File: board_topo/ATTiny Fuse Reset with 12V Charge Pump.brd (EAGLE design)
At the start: 68.6 x 53.3 mm, 59 parts, among them IC1 74HC04D, Q1 BSS138, Q2 PMV65XP, Q3 BSS138, Q4 BSS138, Q5 BSS138, Q6 BSS138, Q7 BSS138, Q8 BSS130, SW3 SWITCH_SPDT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

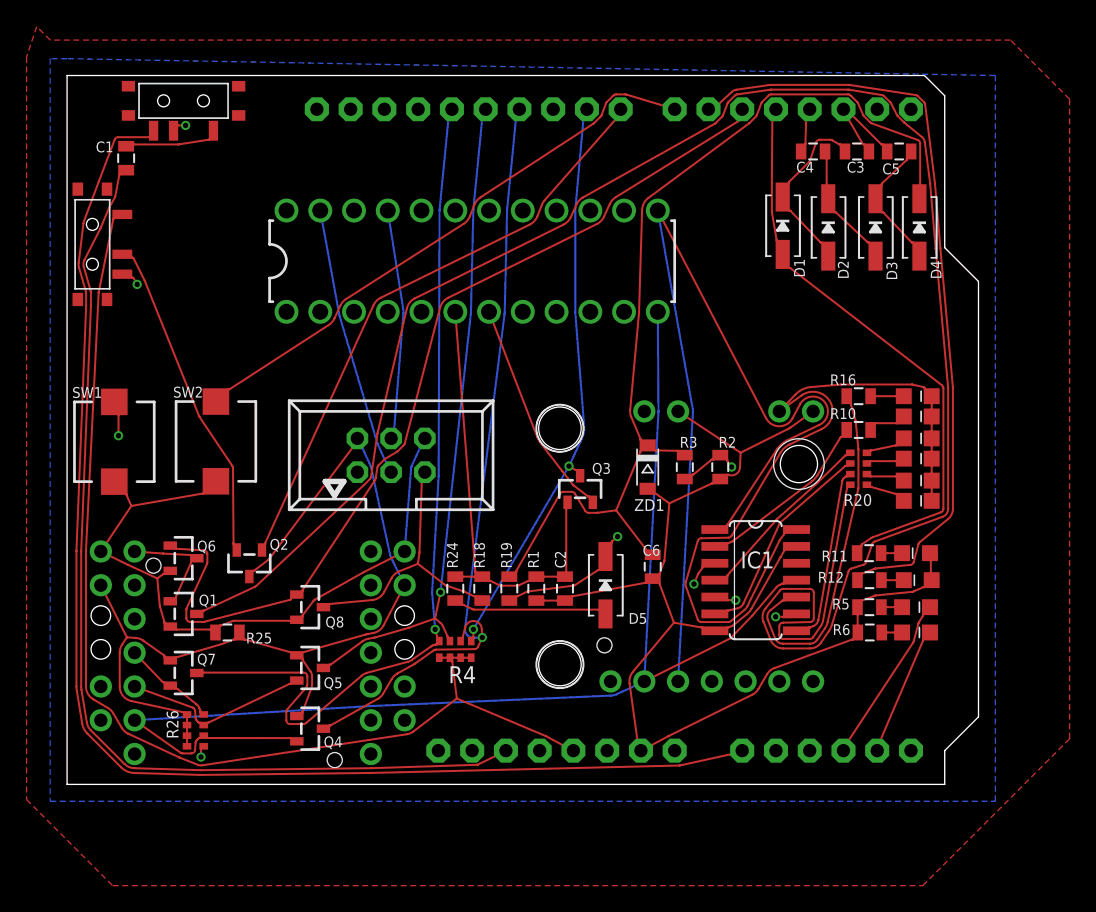
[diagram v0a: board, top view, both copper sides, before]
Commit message: new brd with 4layer, tnames fix
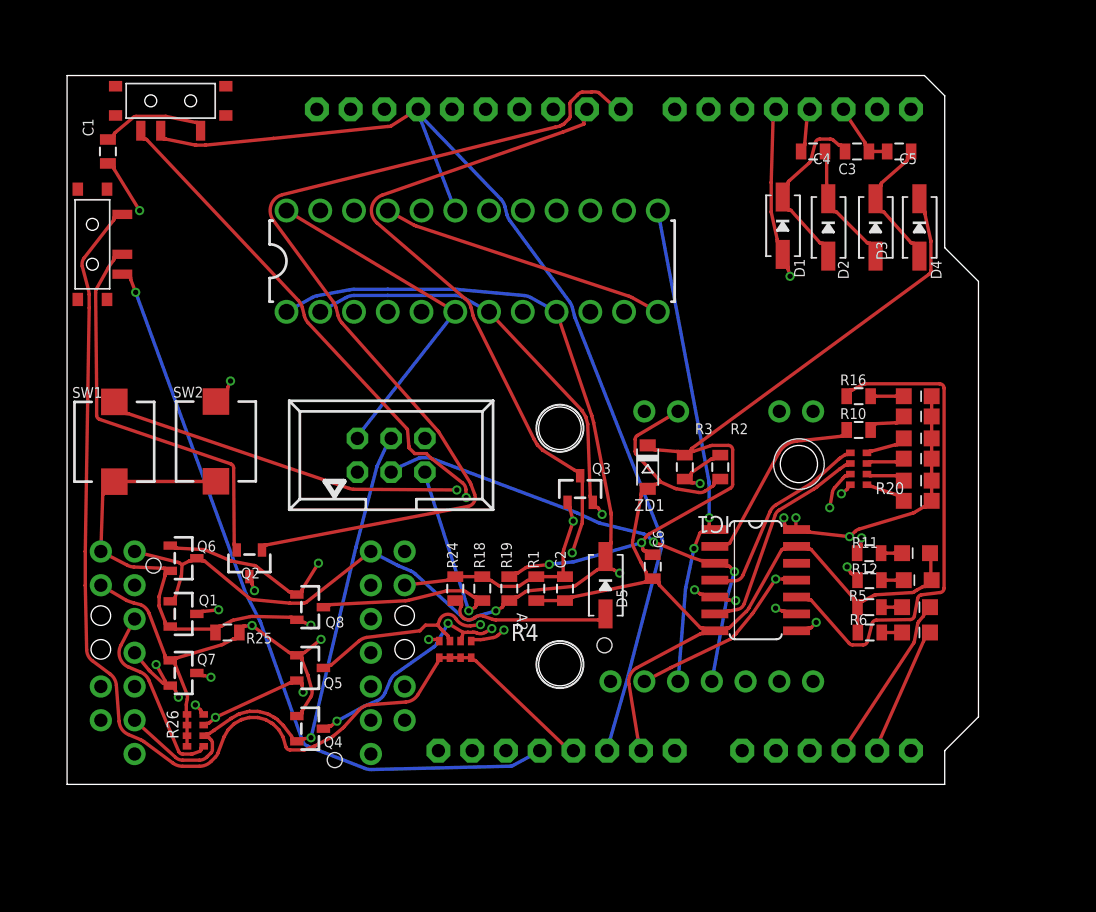
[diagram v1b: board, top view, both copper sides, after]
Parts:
- HV_ON: value HV -> HV on
- ISP: value pmd -> pmode
- PB5: value PB5 -> PB5 rst
- moved C1 1.46 mm to (3.07, 47.6)
- moved SW3 0.97 mm to (7.80, 51.4)
- renumbered HVON to HV_ON
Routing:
- net N$32: track 149.9 -> 51.2 mm, vias 0 -> 2
- net ATTINY_VCC: track 247.7 -> 161.8 mm, vias 0 -> 7
- net SII-MISO: track 150.1 -> 109.0 mm, vias 0 -> 4
- net SCI: track 127.8 -> 91.0 mm, vias 2 -> 3
- net N$3: track 99.2 -> 65.5 mm, vias 0 -> 1
- net VCC_OFF: track 44.6 -> 72.2 mm
- net GND: track 237.6 -> 264.7 mm
- net N$19: track 57.6 -> 36.6 mm, vias 0 -> 1
- net N$33: track 75.8 -> 56.2 mm, vias 0 -> 1
- net SDI_MOSI: track 133.5 -> 115.7 mm, vias 0 -> 2
- net N$2: track 43.5 -> 60.0 mm
- net 11.5V: track 73.7 -> 58.2 mm, vias 0 -> 2
- net HV/RESET: track 117.3 -> 103.1 mm, vias 1 -> 2
- net N$13: track 26.8 -> 38.2 mm
- net PUMP_VCC: track 43.6 -> 33.6 mm, vias 0 -> 2
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- removed copper zone on layer 1, net GND
- removed copper zone on layer 16, net GND
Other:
- board text removed: "ATTiny Fuse Reset with 12V Charge Pump Programmer"
- board text removed: "TAMI.org.il"
- board text removed: "V001 05/08/2015 TAMI.org.il"

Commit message: fixied traces in 4layer board, version in board-topor go to fab
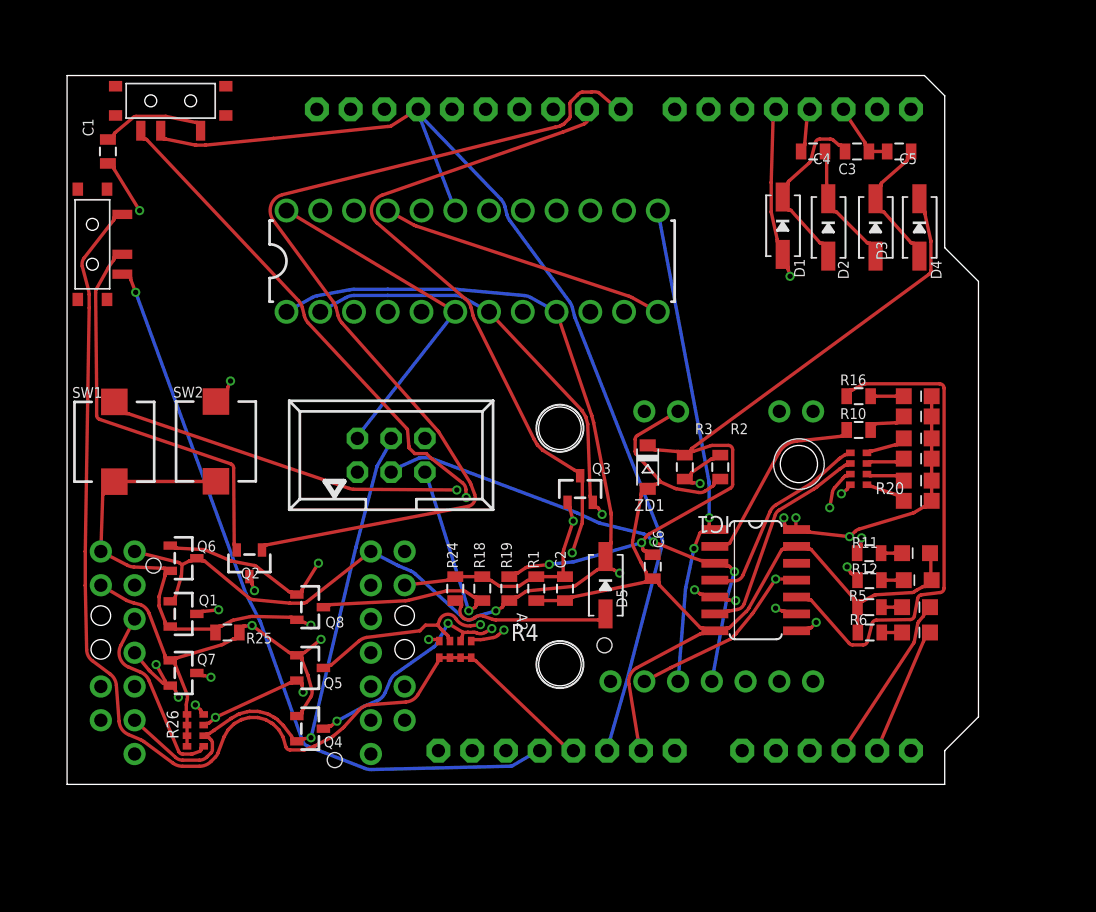
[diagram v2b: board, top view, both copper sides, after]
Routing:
- net GND: track 264.7 -> 271.8 mm
- net ATTINY_VCC: track 161.8 -> 164.2 mm
- net SDO-SCK: track 110.2 -> 112.4 mm
- net SDI_MOSI: track 115.7 -> 117.2 mm
- net N$2: track 60.0 -> 61.0 mm
- net HV_OFF(RESET): track 59.8 -> 60.8 mm
- net P2: track 2.42 -> 3.34 mm
- net N$8: track 56.4 -> 57.3 mm
- net N$37: track 53.3 -> 54.3 mm
- net N$33: track 56.2 -> 57.1 mm
- net N$16: track 55.7 -> 56.6 mm
- net N$19: track 36.6 -> 37.5 mm
- net N$3: track 65.5 -> 66.4 mm
- net P1: track 4.24 -> 5.09 mm
- net N$22: track 44.4 -> 45.2 mm
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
